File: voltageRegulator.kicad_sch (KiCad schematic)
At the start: 5 parts, among them U1801 L78L05_SOT89

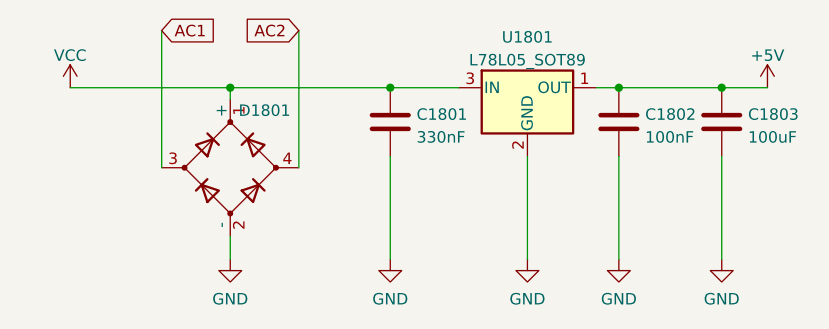
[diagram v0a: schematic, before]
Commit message: added hierarchial labels to some schematics
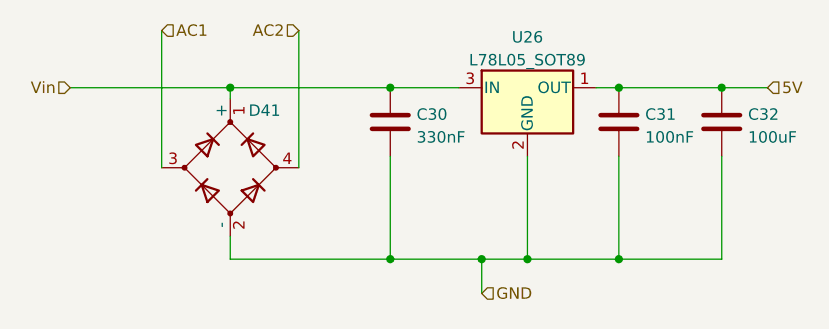
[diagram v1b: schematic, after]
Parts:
- renumbered C1801 to C30, C1802 to C31, C1803 to C32, D1801 to D41, U1801 to U26
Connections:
- net +5V renamed 5V
- net VCC renamed Vin

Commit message: moved some schematic scheets to their own folders and routed a board with it. This allow for re-use of PCB parts.
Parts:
- removed C30: 330nF, Capacitor_SMD:C_0603_1608Metric_Pad1.08x0.95mm_HandSolder, symbol Device:C
- removed C31: 100nF, Capacitor_SMD:C_0603_1608Metric_Pad1.08x0.95mm_HandSolder, symbol Device:C
- removed C32: 100uF, Capacitor_SMD:C_1206_3216Metric_Pad1.33x1.80mm_HandSolder, symbol Device:C
- removed D41: D_Bridge_+-AA, Diode_SMD:Diode_Bridge_Diotec_ABS, symbol Device:D_Bridge_+-AA
- removed U26: L78L05_SOT89, Package_TO_SOT_SMD:SOT-89-3, symbol Regulator_Linear:L78L05_SOT89
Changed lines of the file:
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@@
 (kicad_sch (version 20230121) (generator eeschema)
   (paper "A4")
-  (junction (at 203.2 88.9) (diameter 0) (color 0 0 0 0)
-  )
-  (junction (at 214.63 88.9) (diameter 0) (color 0 0 0 0)
-  )
-  (junction (at 193.04 107.95) (diameter 0) (color 0 0 0 0)
-  )
-  (junction (at 177.8 88.9) (diameter 0) (color 0 0 0 0)
-  )
-  (junction (at 177.8 107.95) (diameter 0) (color 0 0 0 0)
-  )
-  (junction (at 160.02 88.9) (diameter 0) (color 0 0 0 0)
-  )
-  (junction (at 203.2 107.95) (diameter 0) (color 0 0 0 0)
-  )
-  (junction (at 187.96 107.95) (diameter 0) (color 0 0 0 0)
-  )
-  (wire (pts (xy 177.8 88.9) (xy 185.42 88.9))
-    (stroke (width 0) (type default))
-  )
-  (wire (pts (xy 160.02 88.9) (xy 177.8 88.9))
-    (stroke (width 0) (type default))
-  )
-  (wire (pts (xy 203.2 96.52) (xy 203.2 107.95))
-    (stroke (width 0) (type default))
-  )
-  (wire (pts (xy 187.96 107.95) (xy 187.96 111.76))
-    (stroke (width 0) (type default))
-  )
-  (wire (pts (xy 142.24 88.9) (xy 160.02 88.9))
-    (stroke (width 0) (type default))
-  )
-  (wire (pts (xy 187.96 107.95) (xy 193.04 107.95))
-    (stroke (width 0) (type default))
-  )
-  (wire (pts (xy 214.63 96.52) (xy 214.63 107.95))
-    (stroke (width 0) (type default))
-  )
-  (wire (pts (xy 214.63 88.9) (xy 219.71 88.9))
-    (stroke (width 0) (type default))
-  )
-  (wire (pts (xy 160.02 107.95) (xy 177.8 107.95))
-    (stroke (width 0) (type default))
-  )
-  (wire (pts (xy 167.64 82.55) (xy 167.64 97.79))
-    (stroke (width 0) (type default))
-  )
-  (wire (pts (xy 177.8 96.52) (xy 177.8 107.95))
-    (stroke (width 0) (type default))
-  )
-  (wire (pts (xy 160.02 105.41) (xy 160.02 107.95))
-    (stroke (width 0) (type default))
-  )
-  (wire (pts (xy 193.04 96.52) (xy 193.04 107.95))
-    (stroke (width 0) (type default))
-  )
-  (wire (pts (xy 203.2 107.95) (xy 214.63 107.95))
-    (stroke (width 0) (type default))
-  )
-  (wire (pts (xy 152.4 82.55) (xy 152.4 97.79))
-    (stroke (width 0) (type default))
-  )
-  (wire (pts (xy 177.8 107.95) (xy 187.96 107.95))
-    (stroke (width 0) (type default))
-  )
-  (wire (pts (xy 200.66 88.9) (xy 203.2 88.9))
-    (stroke (width 0) (type default))
-  )
-  (wire (pts (xy 160.02 90.17) (xy 160.02 88.9))
-    (stroke (width 0) (type default))
-  )
-  (wire (pts (xy 203.2 88.9) (xy 214.63 88.9))
-    (stroke (width 0) (type default))
-  )
-  (wire (pts (xy 193.04 107.95) (xy 203.2 107.95))
-    (stroke (width 0) (type default))
-  )
-  (hierarchical_label "AC1" (shape input) (at 152.4 82.55 0) (fields_autoplaced)
-    (effects (font (size 1.27 1.27)) (justify left))
-  )
-  (hierarchical_label "GND" (shape input) (at 187.96 111.76 0) (fields_autoplaced)
-    (effects (font (size 1.27 1.27)) (justify left))
-  )
-  (hierarchical_label "Vin" (shape input) (at 142.24 88.9 180) (fields_autoplaced)
-    (effects (font (size 1.27 1.27)) (justify right))
-  )
-  (hierarchical_label "5V" (shape input) (at 219.71 88.9 0) (fields_autoplaced)
-    (effects (font (size 1.27 1.27)) (justify left))
-  )
-  (hierarchical_label "AC2" (shape input) (at 167.64 82.55 180) (fields_autoplaced)
-    (effects (font (size 1.27 1.27)) (justify right))
-  )
-  (symbol (lib_id "Device:C") (at 203.2 92.71 0) (unit 1)
-    (in_bom yes) (on_board yes) (dnp no) (fields_autoplaced)
-    (property "Reference" "C31" (at 206.121 91.8753 0)
-      (effects (font (size 1.27 1.27)) (justify left))
-    )
-    (property "Value" "100nF" (at 206.121 94.4122 0)
-      (effects (font (size 1.27 1.27)) (justify left))
-    )
-    (property "Footprint" "Capacitor_SMD:C_0603_1608Metric_Pad1.08x0.95mm_HandSolder" (at 204.1652 96.52 0)
-      (effects (font (size 1.27 1.27)) hide)
-    )
-    (property "Datasheet" "~" (at 203.2 92.71 0)
-      (effects (font (size 1.27 1.27)) hide)
-    )
-    (property "JLCPCB Part#" "C14663" (at 203.2 92.71 0)
-      (effects (font (size 1.27 1.27)) hide)
-    )
-    (pin "1")
-    (pin "2")
-    (instances
-      (project "general_schematics"
-        (path "/e777d9ec-d073-4229-a9e6-2cf85636e407/4377a106-93b9-41cd-88a1-8112c9568850"
-          (reference "C31") (unit 1)
-        )
-      )
-    )
-  )
-  (symbol (lib_id "Regulator_Linear:L78L05_SOT89") (at 193.04 88.9 0) (unit 1)
-    (in_bom yes) (on_board yes) (dnp no) (fields_autoplaced)
-    (property "Reference" "U26" (at 193.04 83.2952 0)
-      (effects (font (size 1.27 1.27)))
-    )
-    (property "Value" "L78L05_SOT89" (at 193.04 85.8321 0)
-      (effects (font (size 1.27 1.27)))
-    )
-    (property "Footprint" "Package_TO_SOT_SMD:SOT-89-3" (at 193.04 83.82 0)
-      (effects (font (size 1.27 1.27) italic) hide)
-    )
-    (property "Datasheet" "http://www.st.com/content/ccc/resource/technical/document/datasheet/15/55/e5/aa/23/5b/43/fd/CD00000446.pdf/files/CD00000446.pdf/jcr:content/translations/en.CD00000446.pdf" (at 193.04 90.17 0)
-      (effects (font (size 1.27 1.27)) hide)
-    )
-    (property "JLCPCB Part#" "C71136" (at 193.04 88.9 0)
-      (effects (font (size 1.27 1.27)) hide)
-    )
-    (pin "1")
-    (pin "2")
-    (pin "3")
-    (instances
-      (project "general_schematics"
-        (path "/e777d9ec-d073-4229-a9e6-2cf85636e407/4377a106-93b9-41cd-88a1-8112c9568850"
-          (reference "U26") (unit 1)
-        )
-      )
-    )
-  )
-  (symbol (lib_id "Device:D_Bridge_+-AA") (at 160.02 97.79 90) (unit 1)
-    (in_bom yes) (on_board yes) (dnp no)
-    (property "Reference" "D41" (at 163.83 91.44 90)
-      (effects (font (size 1.27 1.27)))
-    )
-    (property "Value" "D_Bridge_+-AA" (at 159.8478 84.4542 0)
-      (effects (font (size 1.27 1.27)) hide)
-    )
-    (property "Footprint" "Diode_SMD:Diode_Bridge_Diotec_ABS" (at 160.02 97.79 0)
-      (effects (font (size 1.27 1.27)) hide)
-    )
-    (property "Datasheet" "~" (at 160.02 97.79 0)
-      (effects (font (size 1.27 1.27)) hide)
-    )
-    (property "JLCPCB Part#" "C2488" (at 160.02 97.79 0)
-      (effects (font (size 1.27 1.27)) hide)
-    )
-    (pin "1")
-    (pin "2")
-    (pin "3")
-    (pin "4")
-    (instances
-      (project "general_schematics"
-        (path "/e777d9ec-d073-4229-a9e6-2cf85636e407/4377a106-93b9-41cd-88a1-8112c9568850"
-          (reference "D41") (unit 1)
-        )
-      )
-    )
-  )
-  (symbol (lib_id "Device:C") (at 177.8 92.71 0) (unit 1)
-    (in_bom yes) (on_board yes) (dnp no) (fields_autoplaced)
-    (property "Reference" "C30" (at 180.721 91.8753 0)
-      (effects (font (size 1.27 1.27)) (justify left))
-    )
-    (property "Value" "330nF" (at 180.721 94.4122 0)
-      (effects (font (size 1.27 1.27)) (justify left))
-    )
-    (property "Footprint" "Capacitor_SMD:C_0603_1608Metric_Pad1.08x0.95mm_HandSolder" (at 178.7652 96.52 0)
-      (effects (font (size 1.27 1.27)) hide)
-    )
-    (property "Datasheet" "~" (at 177.8 92.71 0)
-      (effects (font (size 1.27 1.27)) hide)
-    )
-    (property "JLCPCB Part#" "C1615" (at 177.8 92.71 0)
-      (effects (font (size 1.27 1.27)) hide)
-    )
-    (pin "1")
-    (pin "2")
-    (instances
-      (project "general_schematics"
-        (path "/e777d9ec-d073-4229-a9e6-2cf85636e407/4377a106-93b9-41cd-88a1-8112c9568850"
-          (reference "C30") (unit 1)
-        )
-      )
-    )
-  )
-  (symbol (lib_id "Device:C") (at 214.63 92.71 0) (unit 1)
-    (in_bom yes) (on_board yes) (dnp no) (fields_autoplaced)
-    (property "Reference" "C32" (at 217.551 91.8753 0)
-      (effects (font (size 1.27 1.27)) (justify left))
-    )
-    (property "Value" "100uF" (at 217.551 94.4122 0)
-      (effects (font (size 1.27 1.27)) (justify left))
-    )
-    (property "Footprint" "Capacitor_SMD:C_1206_3216Metric_Pad1.33x1.80mm_HandSolder" (at 215.5952 96.52 0)
-      (effects (font (size 1.27 1.27)) hide)
-    )
-    (property "Datasheet" "~" (at 214.63 92.71 0)
-      (effects (font (size 1.27 1.27)) hide)
-    )
-    (property "JLCPCB Part#" "C15008" (at 214.63 92.71 0)
-      (effects (font (size 1.27 1.27)) hide)
-    )
-    (pin "1")
-    (pin "2")
-    (instances
-      (project "general_schematics"
-        (path "/e777d9ec-d073-4229-a9e6-2cf85636e407/4377a106-93b9-41cd-88a1-8112c9568850"
-          (reference "C32") (unit 1)
-        )
-      )
-    )
-  )
 )
